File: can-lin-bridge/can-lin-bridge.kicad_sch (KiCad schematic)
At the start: 7 parts, among them IC1 PIC18F26Q83T-I_5N, J1 ICSP, U1 TJA1029TK/20/1J, U2 TJA1042TK/3/2Z

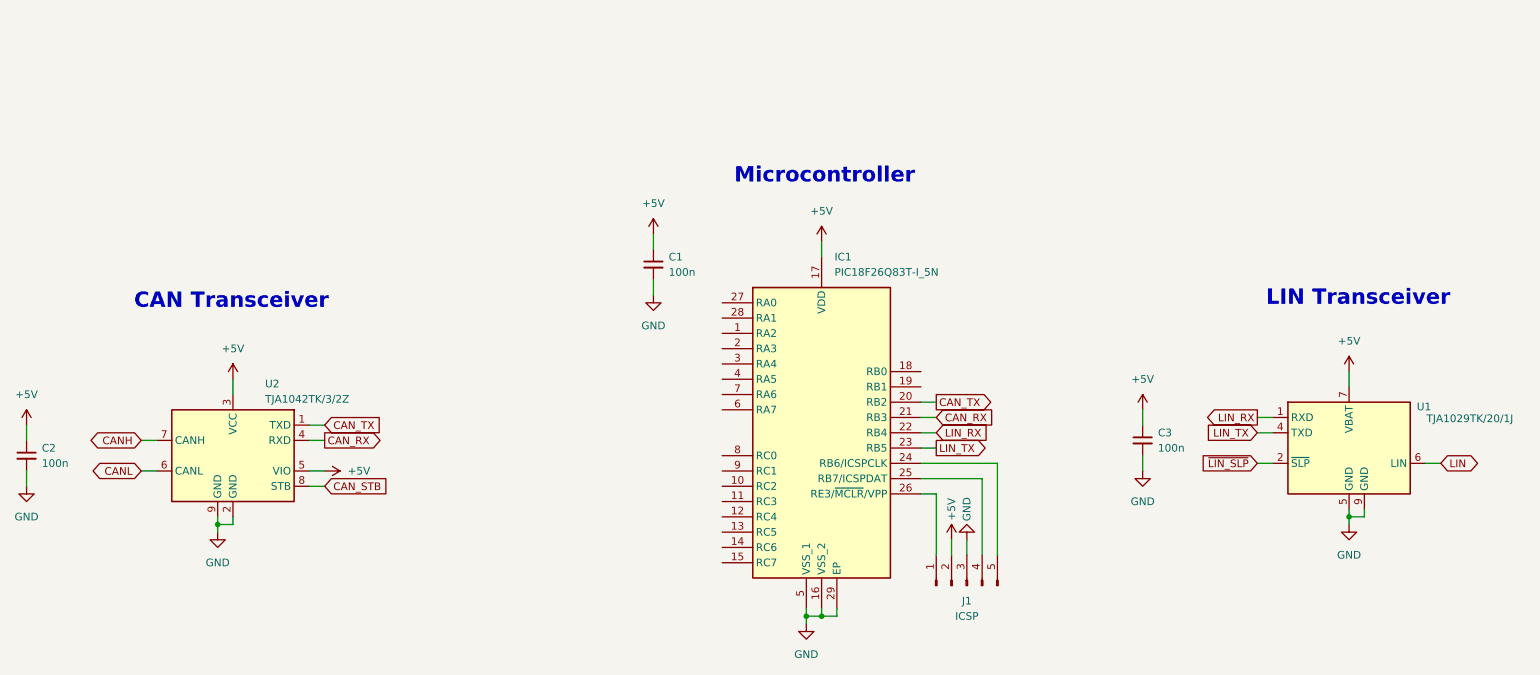
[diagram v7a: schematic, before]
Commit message: can-lin-bridge: Add power indicator and status LEDs
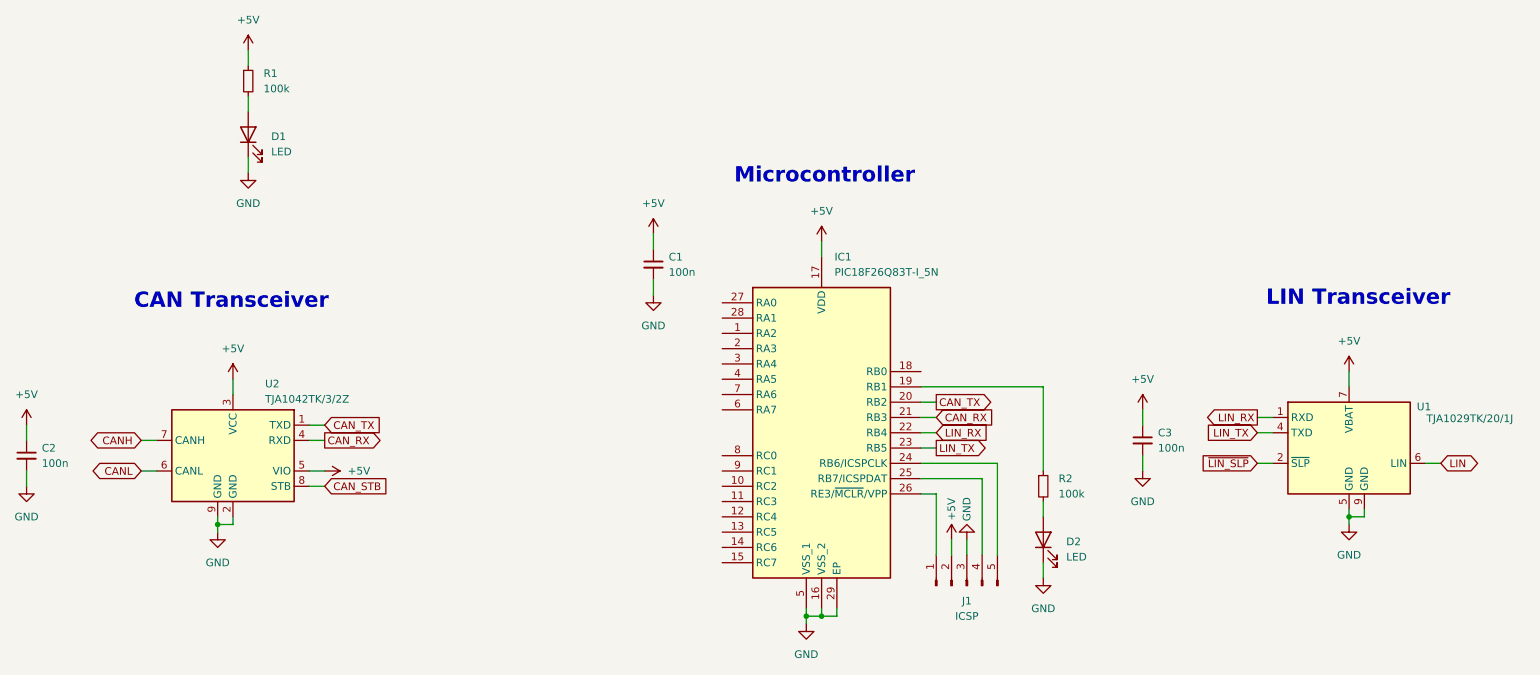
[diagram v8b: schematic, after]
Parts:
- added D1, D2: LED, symbol Device:LED
- added R1, R2: 100k, symbol Device:R_Small
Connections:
- net +5V: now also R1.1
- net GND: now also D1.1 (K), D2.1 (K)
- net at IC1.19 (RB1): now also R2.1
- new net: D1.2 (A), R1.2
- new net: D2.2 (A), R2.2
